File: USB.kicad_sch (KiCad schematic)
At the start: 42 parts, among them J3 USB_C_Receptacle_USB2.0, J4 USB_A_Stacked, SW1 SW_DEBUG_MODE, U2 CP2102N-Axx-xQFN24, U3 FSUSB42MUX, U4 FSUSB42MUX, U5 TPD4EUSB30, U6 USB2422, U7 AP2171W, U8 TPD4EUSB30, Y1 24MHz

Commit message: Select existing standard footprint for USB2422
Signed-off-by: Stefan Agner <stefan@agner.ch>
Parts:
- U6: footprint LightBlue:QFN-24-1EP_4x4mm_P0.5mm_EP2.6x2.6mm -> Package_DFN_QFN:QFN-24-1EP_4x4mm_P0.5mm_EP2.6x2.6mm
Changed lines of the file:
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@@
     (property "Reference" "U6" (id 0) (at 123.19 24.13 0))
     (property "Value" "USB2422" (id 1) (at 120.65 26.67 0))
-    (property "Footprint" "LightBlue:QFN-24-1EP_4x4mm_P0.5mm_EP2.6x2.6mm" (id 2) (at 173.99 102.87 0)
+    (property "Footprint" "Package_DFN_QFN:QFN-24-1EP_4x4mm_P0.5mm_EP2.6x2.6mm" (id 2) (at 173.99 102.87 0)
       (effects (font (size 1.27 1.27)) hide)
     )

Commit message: [WIP] PCB commit
Signed-off-by: Dominik Sliwa <dominik@sliwa.io>
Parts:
- removed C7: 100n, Capacitor_SMD:C_0402_1005Metric, symbol Device:C_Small
- R14: footprint Resistor_SMD:R_0402_1005Metric -> Resistor_SMD:R_1206_3216Metric
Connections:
- net UBS-C.D+ is gone; now on net USB-C.D+: U3.3 (D+)
- net UBS_OTG_ID renamed CM4_USB_OTG_ID
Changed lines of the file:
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@@
   (junction (at 66.04 80.01) (diameter 0.9144) (color 0 0 0 0))
   (junction (at 66.04 88.9) (diameter 0.9144) (color 0 0 0 0))
-  (junction (at 73.66 80.01) (diameter 0.9144) (color 0 0 0 0))
-  (junction (at 73.66 88.9) (diameter 0.9144) (color 0 0 0 0))
   (junction (at 81.28 68.58) (diameter 0.9144) (color 0 0 0 0))
   (junction (at 81.28 74.93) (diameter 0.9144) (color 0 0 0 0))
@@
     (stroke (width 0.1524) (type solid) (color 0 0 0 0))
   )
+  (bus_entry (at 26.67 25.4) (size 2.54 2.54)
+    (stroke (width 0.1524) (type solid) (color 0 0 0 0))
+  )
+  (bus_entry (at 26.67 27.94) (size 2.54 2.54)
+    (stroke (width 0.1524) (type solid) (color 0 0 0 0))
+  )
+  (bus_entry (at 26.67 35.56) (size 2.54 2.54)
+    (stroke (width 0.1524) (type solid) (color 0 0 0 0))
+  )
   (bus_entry (at 26.67 55.88) (size 2.54 2.54)
     (stroke (width 0.1524) (type solid) (color 0 0 0 0))
@@
     (stroke (width 0.1524) (type solid) (color 0 0 0 0))
   )
-  (bus_entry (at 27.94 25.4) (size 2.54 2.54)
-    (stroke (width 0.1524) (type solid) (color 0 0 0 0))
-  )
-  (bus_entry (at 27.94 27.94) (size 2.54 2.54)
-    (stroke (width 0.1524) (type solid) (color 0 0 0 0))
-  )
-  (bus_entry (at 27.94 35.56) (size 2.54 2.54)
-    (stroke (width 0.1524) (type solid) (color 0 0 0 0))
-  )
   (bus_entry (at 69.85 55.88) (size -2.54 2.54)
     (stroke (width 0.1524) (type solid) (color 0 0 0 0))
@@
     (stroke (width 0) (type solid) (color 0 0 0 0))
   )
+  (wire (pts (xy 29.21 27.94) (xy 43.18 27.94))
+    (stroke (width 0) (type solid) (color 0 0 0 0))
+  )
+  (wire (pts (xy 29.21 30.48) (xy 43.18 30.48))
+    (stroke (width 0) (type solid) (color 0 0 0 0))
+  )
+  (wire (pts (xy 29.21 38.1) (xy 43.18 38.1))
+    (stroke (width 0) (type solid) (color 0 0 0 0))
+  )
   (wire (pts (xy 29.21 66.04) (xy 39.37 66.04))
     (stroke (width 0) (type solid) (color 0 0 0 0))
@@
     (stroke (width 0) (type solid) (color 0 0 0 0))
   )
-  (wire (pts (xy 30.48 27.94) (xy 43.18 27.94))
-    (stroke (width 0) (type solid) (color 0 0 0 0))
-  )
-  (wire (pts (xy 30.48 30.48) (xy 43.18 30.48))
-    (stroke (width 0) (type solid) (color 0 0 0 0))
-  )
-  (wire (pts (xy 30.48 38.1) (xy 43.18 38.1))
-    (stroke (width 0) (type solid) (color 0 0 0 0))
-  )
   (wire (pts (xy 30.48 109.22) (xy 33.02 109.22))
     (stroke (width 0) (type solid) (color 0 0 0 0))
@@
     (stroke (width 0) (type solid) (color 0 0 0 0))
   )
+  (wire (pts (xy 66.04 80.01) (xy 82.55 80.01))
+    (stroke (width 0) (type solid) (color 0 0 0 0))
+  )
   (wire (pts (xy 66.04 86.36) (xy 66.04 88.9))
     (stroke (width 0) (type solid) (color 0 0 0 0))
   )
-  (wire (pts (xy 66.04 88.9) (xy 73.66 88.9))
+  (wire (pts (xy 66.04 88.9) (xy 82.55 88.9))
     (stroke (width 0) (type solid) (color 0 0 0 0))
   )
@@
     (stroke (width 0) (type solid) (color 0 0 0 0))
   )
-  (wire (pts (xy 73.66 80.01) (xy 66.04 80.01))
-    (stroke (width 0) (type solid) (color 0 0 0 0))
-  )
-  (wire (pts (xy 73.66 80.01) (xy 73.66 81.28))
-    (stroke (width 0) (type solid) (color 0 0 0 0))
-  )
-  (wire (pts (xy 73.66 86.36) (xy 73.66 88.9))
-    (stroke (width 0) (type solid) (color 0 0 0 0))
-  )
-  (wire (pts (xy 73.66 88.9) (xy 82.55 88.9))
-    (stroke (width 0) (type solid) (color 0 0 0 0))
-  )
   (wire (pts (xy 78.74 74.93) (xy 81.28 74.93))
     (stroke (width 0) (type solid) (color 0 0 0 0))
@@
     (stroke (width 0) (type solid) (color 0 0 0 0))
   )
-  (wire (pts (xy 82.55 80.01) (xy 73.66 80.01))
-    (stroke (width 0) (type solid) (color 0 0 0 0))
-  )
   (wire (pts (xy 82.55 80.01) (xy 82.55 81.28))
     (stroke (width 0) (type solid) (color 0 0 0 0))
@@
     (stroke (width 0) (type solid) (color 0 0 0 0))
   )
-  (bus (pts (xy 25.4 24.13) (xy 27.94 24.13))
+  (bus (pts (xy 24.13 24.13) (xy 26.67 24.13))
+    (stroke (width 0) (type solid) (color 0 0 0 0))
+  )
+  (bus (pts (xy 26.67 24.13) (xy 26.67 25.4))
+    (stroke (width 0) (type solid) (color 0 0 0 0))
+  )
+  (bus (pts (xy 26.67 25.4) (xy 26.67 27.94))
+    (stroke (width 0) (type solid) (color 0 0 0 0))
+  )
+  (bus (pts (xy 26.67 27.94) (xy 26.67 35.56))
     (stroke (width 0) (type solid) (color 0 0 0 0))
   )
@@
   )
   (bus (pts (xy 26.67 58.42) (xy 26.67 55.88))
-    (stroke (width 0) (type solid) (color 0 0 0 0))
-  )
-  (bus (pts (xy 27.94 24.13) (xy 27.94 25.4))
-    (stroke (width 0) (type solid) (color 0 0 0 0))
-  )
-  (bus (pts (xy 27.94 25.4) (xy 27.94 27.94))
-    (stroke (width 0) (type solid) (color 0 0 0 0))
-  )
-  (bus (pts (xy 27.94 27.94) (xy 27.94 35.56))
     (stroke (width 0) (type solid) (color 0 0 0 0))
   )
@@
     (effects (font (size 1.27 1.27)) (justify left bottom))
   )
-  (label "UBS_OTG_ID" (at 31.75 38.1 0)
-    (effects (font (size 1.27 1.27)) (justify left bottom))
-  )
   (label "CP{USB}" (at 31.75 130.81 180)
     (effects (font (size 1.27 1.27)) (justify right bottom))
@@
     (effects (font (size 1.27 1.27)) (justify right bottom))
   )
-  (label "UBS_OTG_ID" (at 36.83 177.8 0)
+  (label "CM4_USB_OTG_ID" (at 34.29 177.8 0)
     (effects (font (size 1.27 1.27)) (justify left bottom))
   )
@@
     (effects (font (size 1.27 1.27)) (justify left bottom))
   )
-  (label "UBS-C.D+" (at 39.37 58.42 180)
+  (label "USB-C.D+" (at 39.37 58.42 180)
     (effects (font (size 1.27 1.27)) (justify right bottom))
   )
@@
     (effects (font (size 1.27 1.27)) (justify right bottom))
   )
+  (label "CM4_USB_OTG_ID" (at 41.91 38.1 180)
+    (effects (font (size 1.27 1.27)) (justify right bottom))
+  )
   (label "CP.D+" (at 59.69 58.42 0)
     (effects (font (size 1.27 1.27)) (justify left bottom))
@@
     (effects (font (size 1.27 1.27)) (justify left bottom))
   )
-  (hierarchical_label "{CM4_USB}" (shape bidirectional) (at 25.4 24.13 180)
+  (hierarchical_label "{CM4_USB}" (shape bidirectional) (at 24.13 24.13 180)
     (effects (font (size 1.27 1.27)) (justify right))
   )
@@
     (property "Reference" "R14" (id 0) (at 227.4632 111.76 0))
     (property "Value" "0R" (id 1) (at 236.112 114.3 0))
-    (property "Footprint" "Resistor_SMD:R_0402_1005Metric" (id 2) (at 229.87 114.3 0)
+    (property "Footprint" "Resistor_SMD:R_1206_3216Metric" (id 2) (at 229.87 114.3 0)
       (effects (font (size 1.27 1.27)) hide)
     )
@@
       (effects (font (size 1.27 1.27)) hide)
     )
-  )
-  (symbol (lib_id "Device:C_Small") (at 73.66 83.82 0) (unit 1)
-    (in_bom yes) (on_board yes)
-    (property "Reference" "C7" (id 0) (at 75.9842 82.6706 0)
-      (effects (font (size 1.27 1.27)) (justify left))
-    )
-    (property "Value" "100n" (id 1) (at 75.984 84.969 0)
-      (effects (font (size 1.27 1.27)) (justify left))
-    )
-    (property "Footprint" "Capacitor_SMD:C_0402_1005Metric" (id 2) (at 73.66 83.82 0)
-      (effects (font (size 1.27 1.27)) hide)
-    )
-    (property "Datasheet" "~" (id 3) (at 73.66 83.82 0)
-      (effects (font (size 1.27 1.27)) hide)
-    )

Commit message: Change TPD4EUSB30 symbol for pass-through routing
Make the pads next to each input pad a passive connection as well to
allow pass-through routing.

Signed-off-by: Stefan Agner <stefan@agner.ch>
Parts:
- U5, U8: symbol Power_Protection:TPD4EUSB30 -> LightBlue:TPD4EUSB30
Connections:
- net USB-C.D+: now also U5.10 (D1+)
- net USB-C.D-: now also U5.9 (D1-)
- net USB0.D+: now also U8.7 (D2+)
- net USB0.D-: now also U8.6 (D2-)
- net USB1.D+: now also U8.10 (D1+)
- net USB1.D-: now also U8.9 (D1-)
- net VBUS_{IN}: now also U5.7 (D2+)
- net at U5.5 (D2-): now also U5.6 (D2-)
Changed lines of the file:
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@@
     (comment 2 "Light Blue")
   )
+  (bus_alias "I2C" (members "SDA" "SCL"))
+  (bus_alias "USB" (members "D+" "D-"))
   (bus_alias "CM4_USB" (members "CM4_USB_D+" "CM4_USB_D-" "CM4_USB_OTG_ID"))
-  (bus_alias "USB" (members "D+" "D-"))
-  (bus_alias "I2C" (members "SDA" "SCL"))
   (junction (at 22.86 80.01) (diameter 0.9144) (color 0 0 0 0))
   (junction (at 22.86 88.9) (diameter 0.9144) (color 0 0 0 0))
@@
     )
   )
-  (symbol (lib_id "Power_Protection:TPD4EUSB30") (at 138.43 181.61 0) (unit 1)
+  (symbol (lib_name "LightBlue:TPD4EUSB30_1") (lib_id "LightBlue:TPD4EUSB30") (at 138.43 181.61 0) (unit 1)
     (in_bom yes) (on_board yes)
     (property "Reference" "U5" (id 0) (at 138.43 168.91 0))
@@
     )
   )
-  (symbol (lib_id "Power_Protection:TPD4EUSB30") (at 243.84 142.24 0) (unit 1)
+  (symbol (lib_id "LightBlue:TPD4EUSB30") (at 243.84 142.24 0) (unit 1)
     (in_bom yes) (on_board yes)
     (property "Reference" "U8" (id 0) (at 243.84 129.54 0))

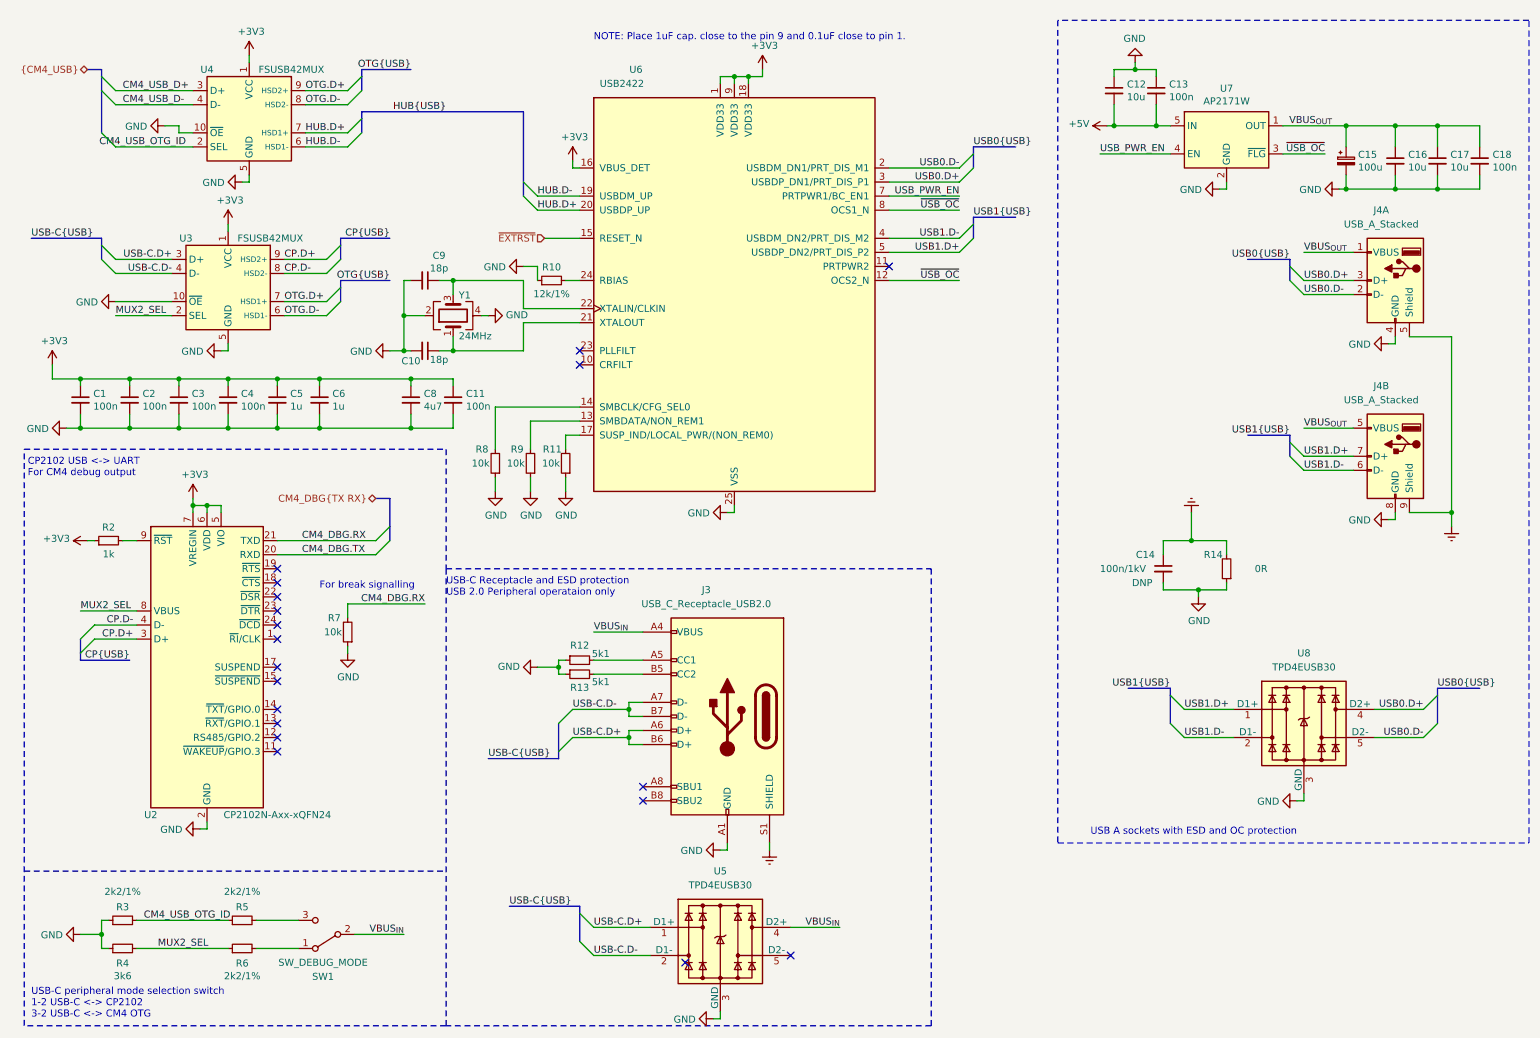
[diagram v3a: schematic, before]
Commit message: PCB[WIP]/SCH:
changes:
-more routing
-added poe negotiation disabled when +12V is present on the DC jack
-modified m.2 "holes"

Signed-off-by: Dominik Sliwa <dominik@sliwa.io>
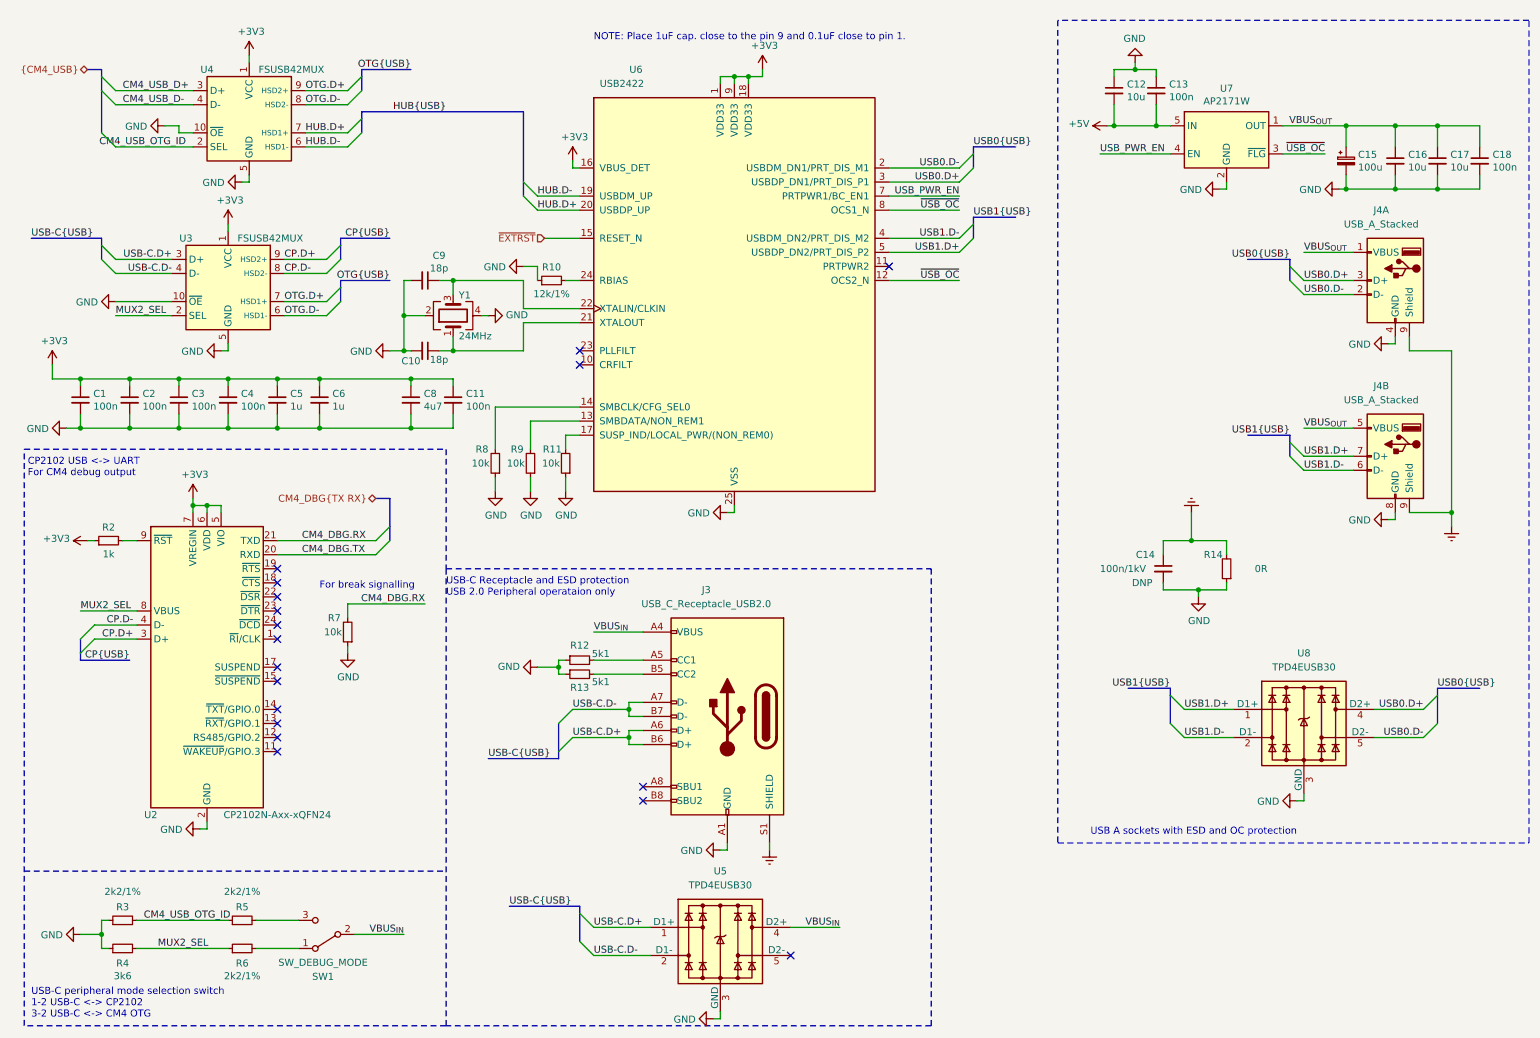
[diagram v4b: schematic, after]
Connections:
- net Earth: now also J4.9 (Shield); no longer J4.5 (Shield)
- no-connect marks 19 -> 18
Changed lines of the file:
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@@
   (no_connect (at 124.46 153.67))
   (no_connect (at 124.46 156.21))
-  (no_connect (at 132.08 185.42))
   (no_connect (at 151.13 184.15))
   (no_connect (at 168.91 59.69))
@@
     (stroke (width 0) (type solid) (color 0 0 0 0))
   )
-  (wire (pts (xy 262.89 72.39) (xy 270.51 72.39))
+  (wire (pts (xy 262.89 72.39) (xy 262.89 74.93))
+    (stroke (width 0) (type solid) (color 0 0 0 0))
+  )
+  (wire (pts (xy 262.89 74.93) (xy 270.51 74.93))
     (stroke (width 0) (type solid) (color 0 0 0 0))
   )
@@
     (stroke (width 0) (type solid) (color 0 0 0 0))
   )
-  (wire (pts (xy 270.51 72.39) (xy 270.51 104.14))
+  (wire (pts (xy 270.51 74.93) (xy 270.51 104.14))
     (stroke (width 0) (type solid) (color 0 0 0 0))
   )
@@
     )
   )
-  (symbol (lib_id "LightBlue:USB_A_Stacked") (at 260.35 62.23 0) (mirror y) (unit 1)
+  (symbol (lib_name "LightBlue:USB_A_Stacked_1") (lib_id "LightBlue:USB_A_Stacked") (at 260.35 62.23 0) (mirror y) (unit 1)
     (in_bom yes) (on_board yes)
     (property "Reference" "J4" (id 0) (at 257.81 49.53 0))

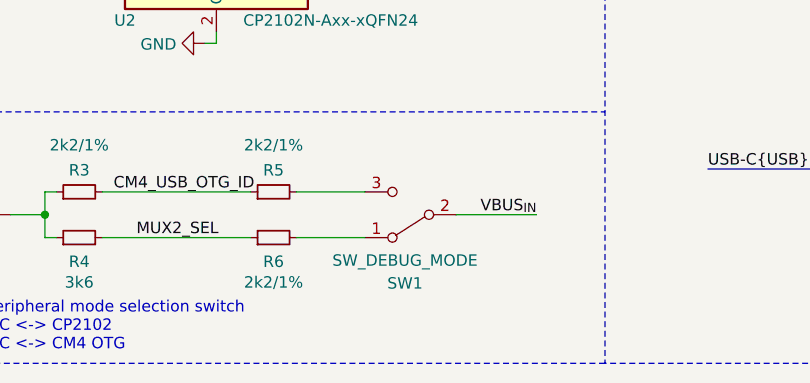
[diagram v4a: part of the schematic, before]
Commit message: Improve SW and D (LED) ordering and silkscreen
Make sure switches (SW) are ordered logically. Also use D1 through D6
for LEDs.

Signed-off-by: Stefan Agner <stefan@agner.ch>
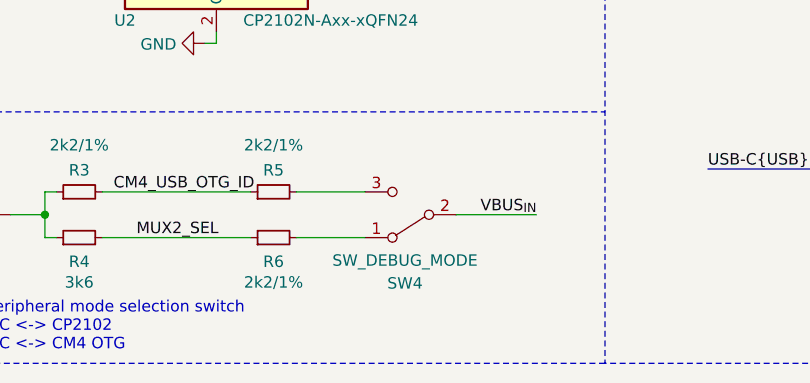
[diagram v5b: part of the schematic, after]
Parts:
- renumbered SW1 to SW4
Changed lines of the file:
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@@
     (comment 2 "Light Blue")
   )
+  (bus_alias "CM4_USB" (members "CM4_USB_D+" "CM4_USB_D-" "CM4_USB_OTG_ID"))
+  (bus_alias "USB" (members "D+" "D-"))
   (bus_alias "I2C" (members "SDA" "SCL"))
-  (bus_alias "USB" (members "D+" "D-"))
-  (bus_alias "CM4_USB" (members "CM4_USB_D+" "CM4_USB_D-" "CM4_USB_OTG_ID"))
   (junction (at 22.86 80.01) (diameter 0.9144) (color 0 0 0 0))
   (junction (at 22.86 88.9) (diameter 0.9144) (color 0 0 0 0))
@@
   (symbol (lib_id "Switch:SW_SPDT") (at 67.31 180.34 180) (unit 1)
     (in_bom yes) (on_board yes)
-    (property "Reference" "SW1" (id 0) (at 66.675 187.96 0))
+    (property "Reference" "SW4" (id 0) (at 66.675 187.96 0))
     (property "Value" "SW_DEBUG_MODE" (id 1) (at 66.675 185.42 0))
     (property "Footprint" "Button_Switch_SMD:SW_SPDT_PCM12" (id 2) (at 67.31 180.34 0)

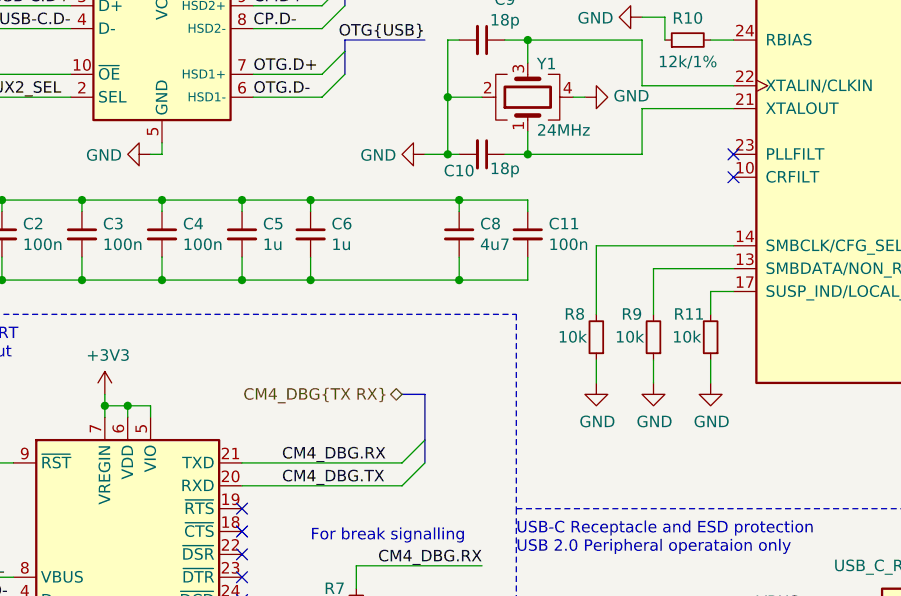
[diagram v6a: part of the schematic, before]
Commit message: USB.kicad_sch: Add CRFILT cap and adjust resistors
CRFILT capacitor is required for the chip to start properly
and 10k pull-downs were too strong according to the datasheet.

Signed-off-by: Dominik Sliwa <dominik@sliwa.io>
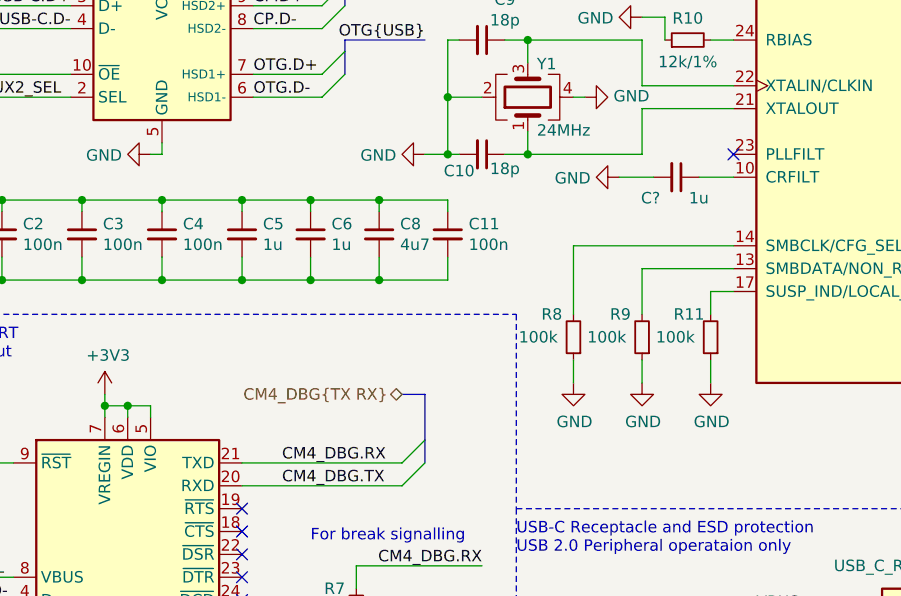
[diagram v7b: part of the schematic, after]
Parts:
- added C?: 1u, Capacitor_SMD:C_0402_1005Metric, symbol Device:C_Small
- R11, R8, R9: value 10k -> 100k
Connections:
- net GND: now also C?.2
- net at U6.10 (CRFILT): now also C?.1
- no-connect marks 18 -> 17
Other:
- moved on the sheet: C11, C8, R8, R9
